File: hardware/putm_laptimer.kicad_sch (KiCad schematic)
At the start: 43 parts, among them J1 Conn_01x22, J10 Conn_01x07, J11 Conn_01x07, J2 Conn_01x22, J3 Conn_01x22, J4 Conn_01x22, J5 2091-1372, J6 2091-1372, J7 Conn_02x05_Odd_Even, J8 Conn_01x09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

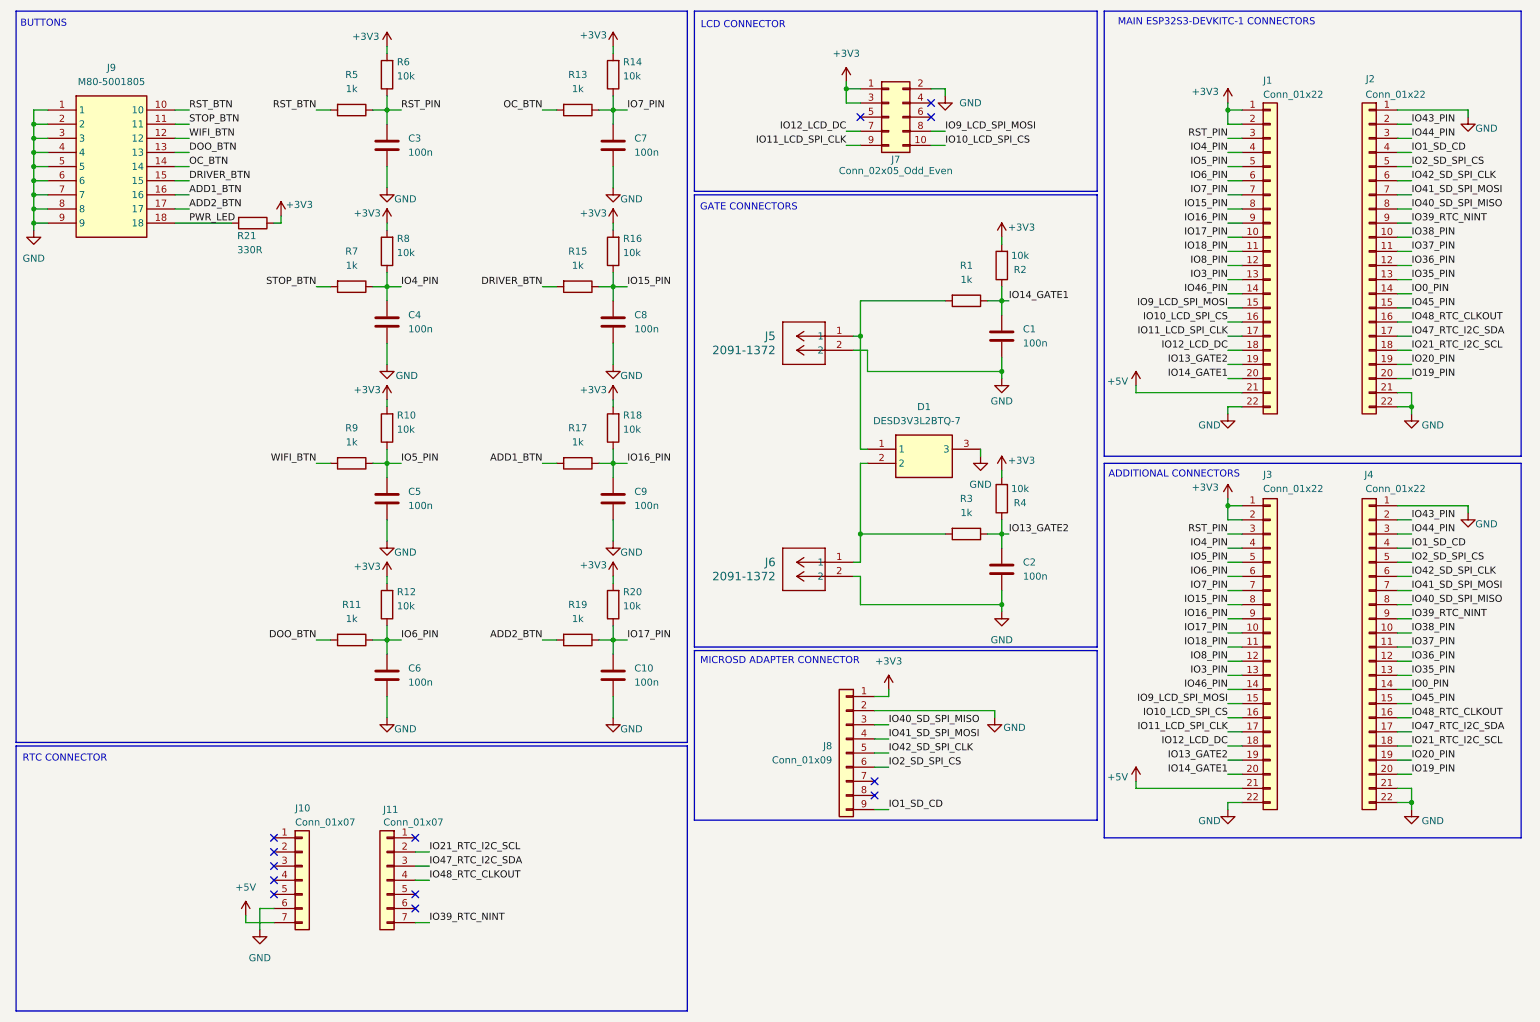
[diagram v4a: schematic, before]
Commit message: Added connectors for step-up converter and changed wago connectors to 6-pin
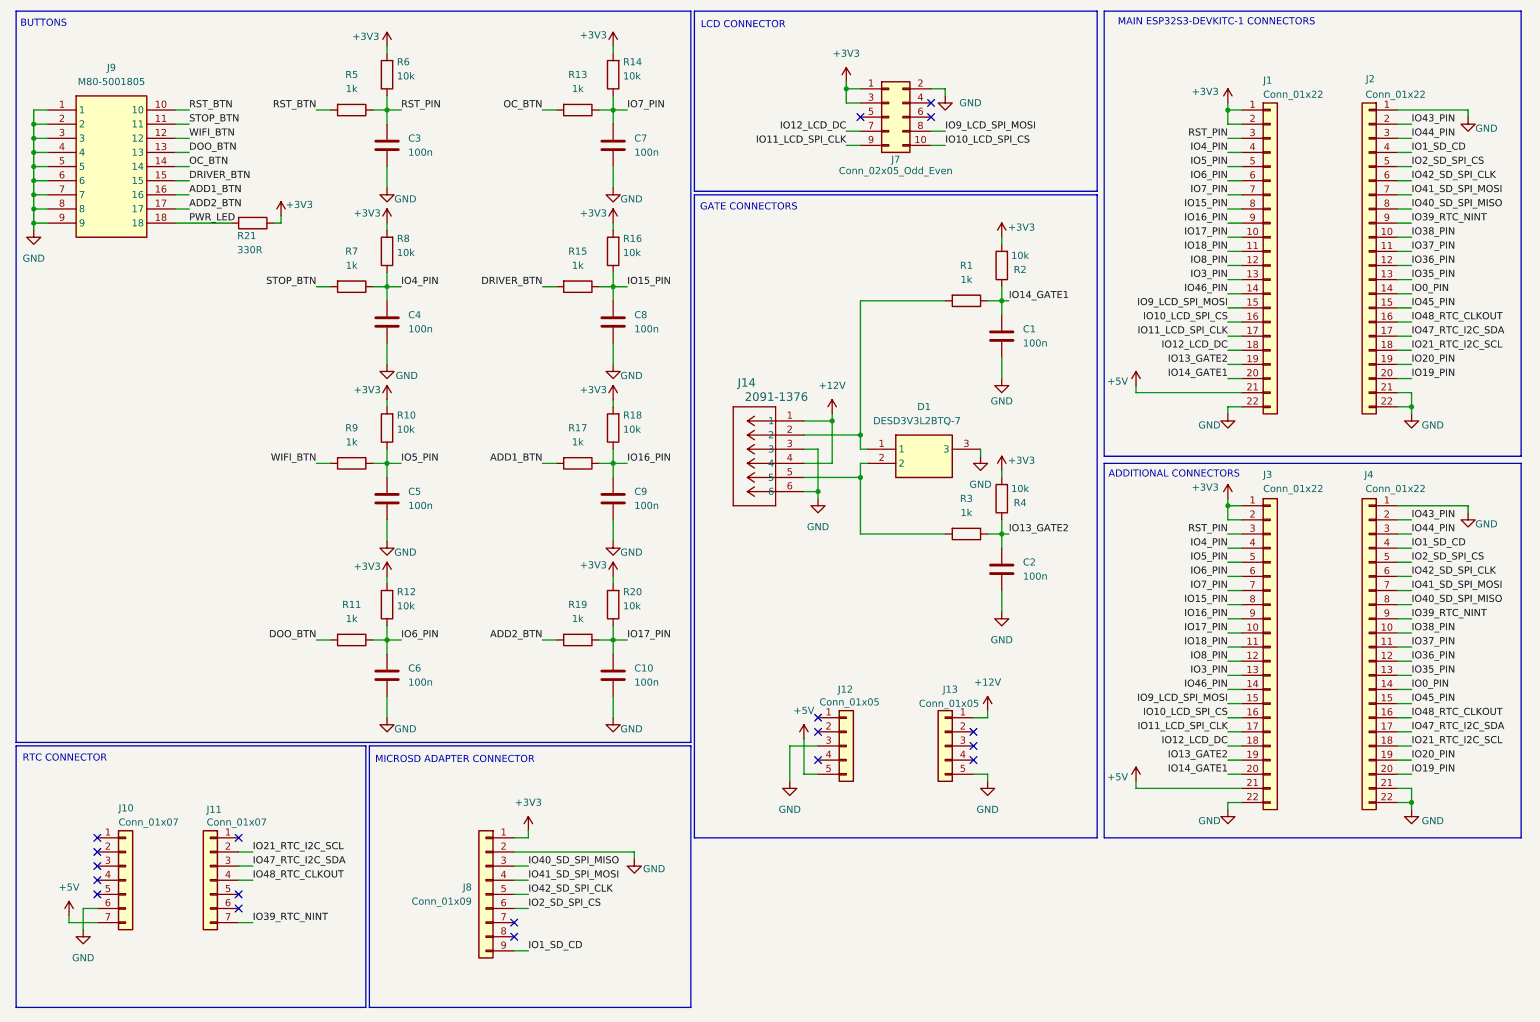
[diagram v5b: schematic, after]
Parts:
- removed J5, J6: 2091-1372, Footprint:CONN2_2091-1372_WAG, symbol 2026-01-10_16-31-44:2092-1372
- added J12, J13: Conn_01x05, Connector_PinSocket_2.00mm:PinSocket_1x05_P2.00mm_Vertical, symbol Connector_Generic:Conn_01x05
- added J14: 2091-1376, CONN6_2091-1376_WAG, symbol 2026-01-25_23-06-05:2091-1376
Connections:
- net +5V: now also J12.5 (Pin_5)
- net GND: now also J12.3 (Pin_3), J13.5 (Pin_5), J14.3, J14.6
- net at D1.1, R1.2: now also J14.2
- net at D1.2, R3.2: now also J14.5
- new net +12V: J13.1 (Pin_1), J14.1, J14.4
- no-connect marks 13 -> 19
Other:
- moved on the sheet: J10, J11, J8

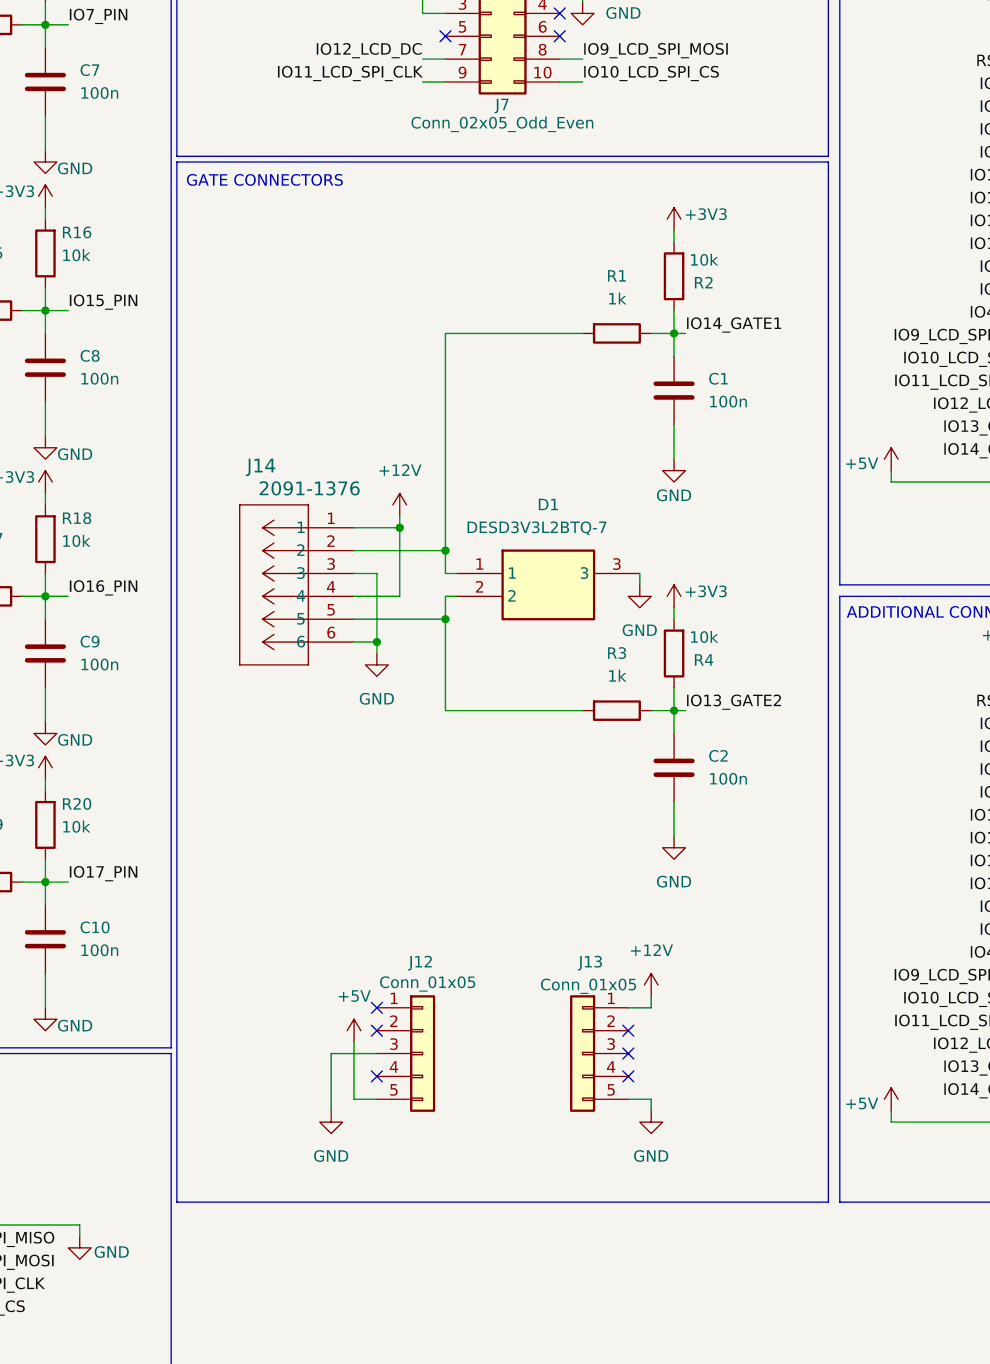
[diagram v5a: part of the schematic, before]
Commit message: Fixed connector footprint
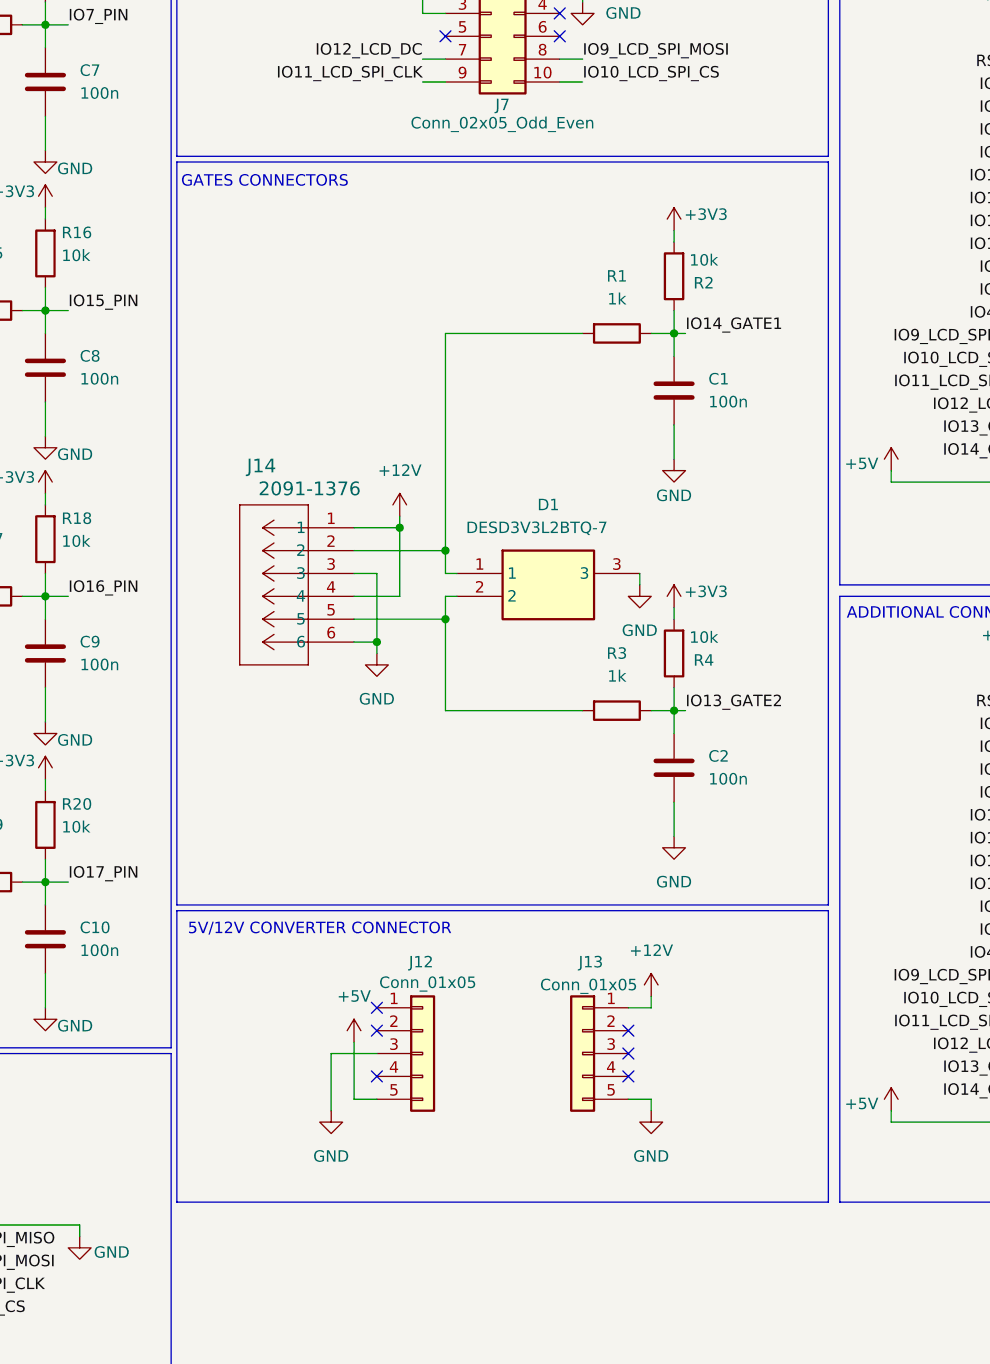
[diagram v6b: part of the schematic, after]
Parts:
- J14: footprint CONN6_2091-1376_WAG -> Footprint:CONN6_2091-1376_WAG
- J7: footprint Connector_PinHeader_2.00mm:PinHeader_2x05_P2.00mm_Vertical_SMD -> Connector_PinHeader_2.54mm:PinHeader_2x05_P2.54mm_Vertical_SMD
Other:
- note added: "5V/12V CONVERTER CONNECTOR"
- note added: "GATES CONNECTORS"
- note removed: "GATE CONNECTORS"
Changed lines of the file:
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@@
 	(rectangle
 		(start 135.255 46.99)
-		(end 207.645 162.56)
+		(end 207.645 129.54)
 		(stroke
 			(width 0)
@@
 		)
 	)
+	(rectangle
+		(start 135.255 130.175)
+		(end 207.645 162.56)
+		(stroke
+			(width 0)
+			(type default)
+		)
+		(fill
+			(type none)
+		)
+	)
 	(text "MAIN ESP32S3-DEVKITC-1 CONNECTORS"
 		(exclude_from_sim no)
@@
 		)
 	)
-	(text "GATE CONNECTORS\n"
+	(text "GATES CONNECTORS"
 		(exclude_from_sim no)
 		(at 145.034 49.276 0)
@@
 		)
 	)
+	(text "5V/12V CONVERTER CONNECTOR\n"
+		(exclude_from_sim no)
+		(at 151.13 132.334 0)
+		(effects
+			(font
+				(size 1.27 1.27)
+			)
+		)
+	)
 	(text "MICROSD ADAPTER CONNECTOR\n"
 		(exclude_from_sim no)
@@
 			)
 		)
-		(property "Footprint" "Connector_PinHeader_2.00mm:PinHeader_2x05_P2.00mm_Vertical_SMD"
+		(property "Footprint" "Connector_PinHeader_2.54mm:PinHeader_2x05_P2.54mm_Vertical_SMD"
 			(at 170.18 33.02 0)
 			(effects
@@
 			)
 		)
-		(property "Footprint" "CONN6_2091-1376_WAG"
+		(property "Footprint" "Footprint:CONN6_2091-1376_WAG"
 			(at 154.94 87.63 0)
 			(effects
